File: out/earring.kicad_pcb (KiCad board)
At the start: 6 copper layers, 30.5 x 35.8 mm, 120 parts, among them J1 USB-C, SW1 BOOTSEL, SW2 PWR, U1 RP2354A, U2 LGS4056H, U3 NCP730-3.3, U4 TPS22913, U5 USBLC6-2P6, U6 LSM6DS3TR-C, Y1 12MHz

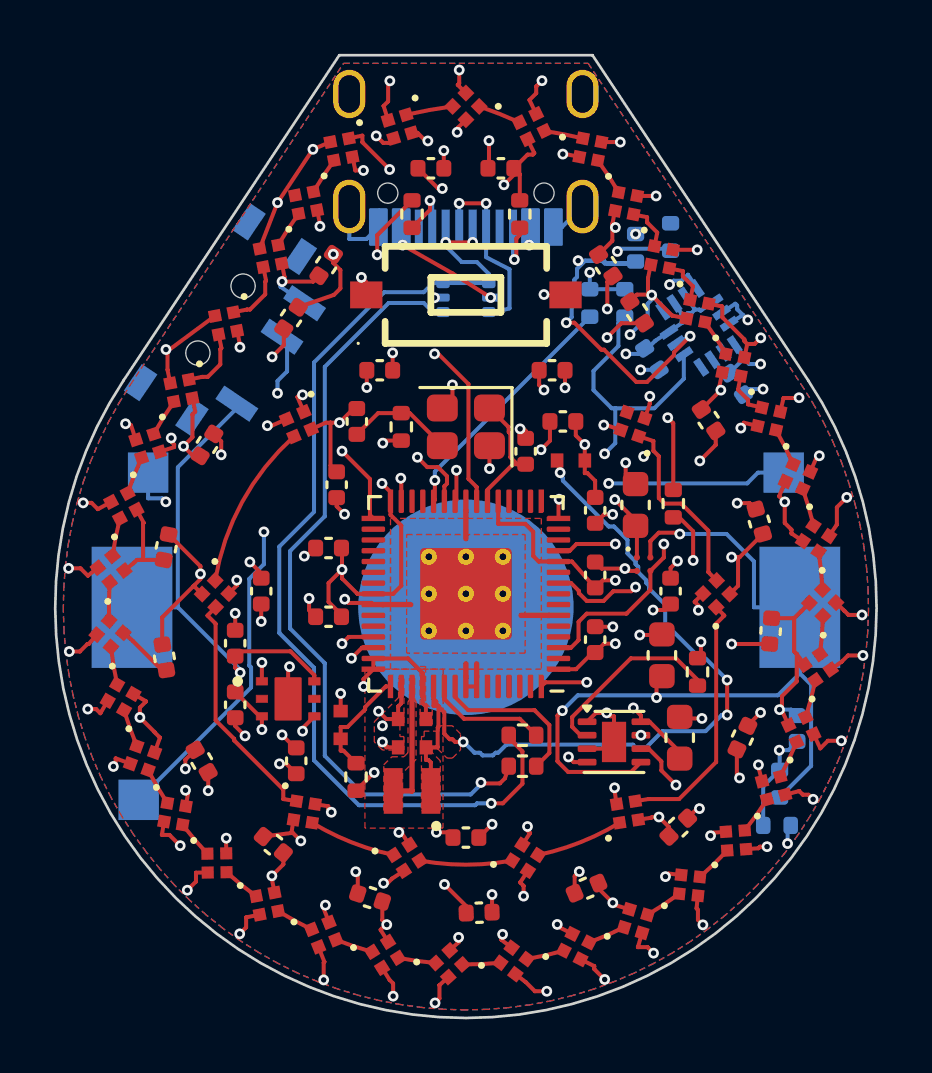
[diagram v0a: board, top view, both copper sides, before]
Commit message: PARTIAL 4-layer board: 0 DRC errors, 8 nets left to hand-route
*** This board is NOT fully routed. It is the best of 6 auto-routing
*** attempts and is handed over for manual completion. See
*** docs/PUNCHLIST-4layer.md.

- design.yaml: layers 4 (was 6) for JLC lead time. The whole pipeline
  switches on board.layers now — route.py (In3/In4 zones, In2 annulus
  hole pulled to r9.35 + 3V3 disc to r9.15 so the interior LED ring
  still gets a plane drop), finish.py (per-stackup plane bands),
  render.py + export.py (layer lists). Set it back to 6 to fall back.
- finish.py: keep_if_best() snapshots the best attempt to
  out/earring-best{.kicad_pcb,.json}. build.py re-rolls the freerouting
  seed on failure and overwrote the board every attempt, so the LAST
  result survived rather than the best one — which is precisely the
  thing worth keeping when a stackup can't be closed automatically.
  build.py clears stale snapshots at the start of a run so a previous
  netlist's score can't veto this one's.
- The In3 east-pour polygon is now defined once in finish.py and
  imported by route.py (was duplicated with a 'keep in sync' comment).

Attempts: 9 / 8 / 11 / 8 / 11 / 11 unconnected, all 0 errors. Stranded:
the three QSPI signals that lost the In3 layer (SD0/SD1/SCLK), the two
back-to-front hops that also used it (LED_EN, IMU_INT1), and three short
local ones (USB_DM, USB_DP, XIN).

Co-Authored-By: Claude Fable 5 <noreply@anthropic.com>
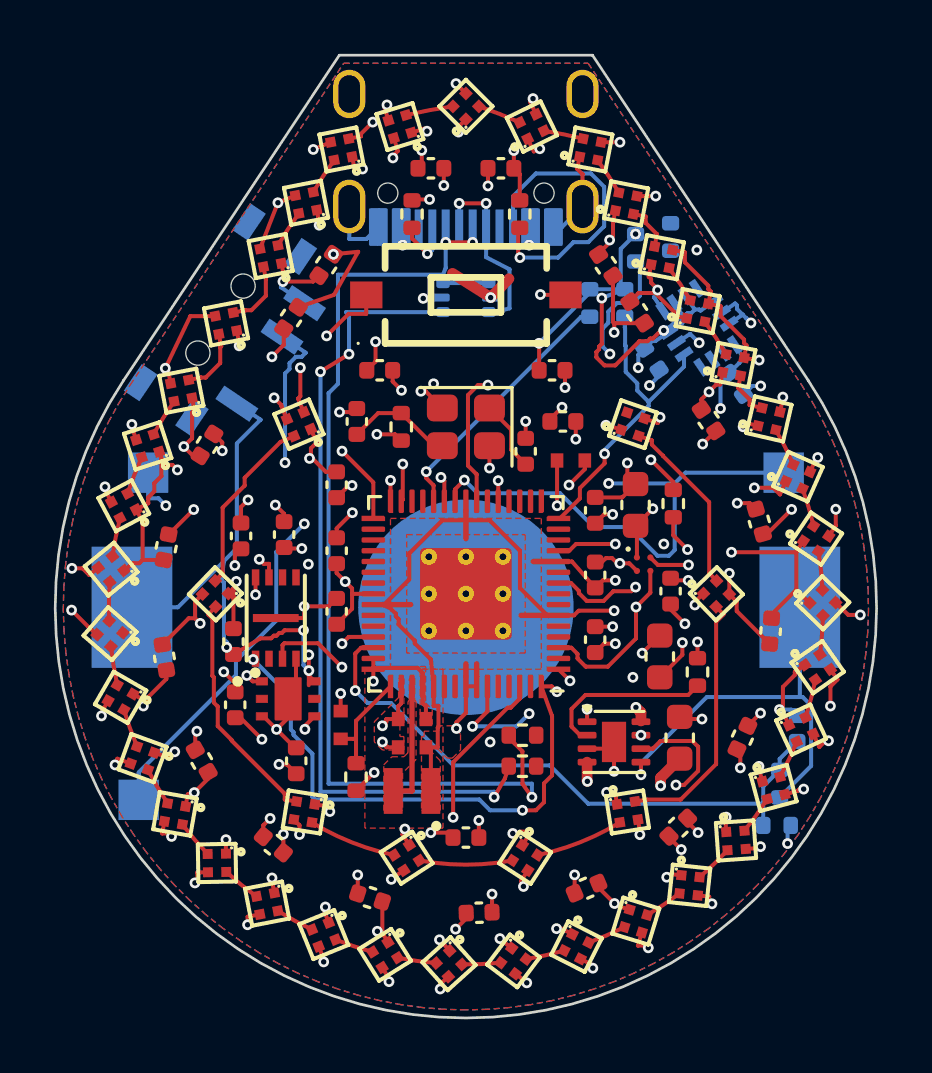
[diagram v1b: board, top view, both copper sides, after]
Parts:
- added C25: 100n, C_0402_1005Metric, F.Cu at (93.2, 97.3)
- added U7: W25Q16JVUXIQ, USON-8_L3.0-W2.0-P0.50-BL-EP, F.Cu at (92.9, 100.4)
- LED1, LED10, LED11, LED12, LED13, LED14, LED15, LED16, LED17, LED18, LED19, LED2, LED20, LED21, LED22, LED23, LED24, LED25, LED26, LED27, LED28, LED29, LED3, LED30, LED31, LED32, LED33, LED34, LED35, LED36, LED37, LED38, LED39, LED4, LED40, LED41, LED42, LED43, LED44, LED45, LED5, LED6, LED7, LED8, LED9: value TBA-C1010MB -> SK6805-EC10; footprint LED_TBA-C1010MB -> LED_SK6805-EC10
- U1: value RP2354A -> RP2350A
- moved C68 2.18 mm to (91.7, 97.3)
- moved C5 0.36 mm to (95.2, 100.2), turned to 90 degrees
- moved C3 0.32 mm to (95.2, 97.9), turned to 90 degrees
- moved C17 0.09 mm to (107.2, 101.8)
- moved C18 0.09 mm to (91.4, 101.3)
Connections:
- LED1 pad 1: LED_D0 -> GND
- LED1 pad 2: VLED -> LED_D0
- LED1 pad 3: GND -> VLED
- LED10 pad 1: LED_D9 -> GND
- LED10 pad 2: VLED -> LED_D9
- LED10 pad 3: GND -> VLED
- LED11 pad 1: LED_D10 -> GND
- LED11 pad 2: VLED -> LED_D10
- LED11 pad 3: GND -> VLED
- LED12 pad 1: LED_D11 -> GND
- LED12 pad 2: VLED -> LED_D11
- LED12 pad 3: GND -> VLED
- LED13 pad 1: LED_D12 -> GND
- LED13 pad 2: VLED -> LED_D12
- LED13 pad 3: GND -> VLED
- LED14 pad 1: LED_D13 -> GND
- LED14 pad 2: VLED -> LED_D13
- LED14 pad 3: GND -> VLED
- LED15 pad 1: LED_D14 -> GND
- LED15 pad 2: VLED -> LED_D14
- LED15 pad 3: GND -> VLED
- LED16 pad 1: LED_D15 -> GND
- LED16 pad 2: VLED -> LED_D15
- LED16 pad 3: GND -> VLED
- LED17 pad 1: LED_D16 -> GND
- LED17 pad 2: VLED -> LED_D16
- LED17 pad 3: GND -> VLED
- LED18 pad 1: LED_D17 -> GND
- LED18 pad 2: VLED -> LED_D17
- LED18 pad 3: GND -> VLED
- LED19 pad 1: LED_D18 -> GND
- LED19 pad 2: VLED -> LED_D18
- LED19 pad 3: GND -> VLED
- LED2 pad 1: LED_D1 -> GND
- LED2 pad 2: VLED -> LED_D1
- LED2 pad 3: GND -> VLED
- LED20 pad 1: LED_D19 -> GND
- LED20 pad 2: VLED -> LED_D19
- LED20 pad 3: GND -> VLED
- LED21 pad 1: LED_D20 -> GND
- LED21 pad 2: VLED -> LED_D20
- LED21 pad 3: GND -> VLED
- LED22 pad 1: LED_D21 -> GND
- LED22 pad 2: VLED -> LED_D21
- LED22 pad 3: GND -> VLED
- LED23 pad 1: LED_D22 -> GND
- LED23 pad 2: VLED -> LED_D22
- LED23 pad 3: GND -> VLED
- LED24 pad 1: LED_D23 -> GND
- LED24 pad 2: VLED -> LED_D23
- LED24 pad 3: GND -> VLED
- LED25 pad 1: LED_D24 -> GND
- LED25 pad 2: VLED -> LED_D24
- LED25 pad 3: GND -> VLED
- LED26 pad 1: LED_D25 -> GND
- LED26 pad 2: VLED -> LED_D25
- LED26 pad 3: GND -> VLED
- LED27 pad 1: LED_D26 -> GND
- LED27 pad 2: VLED -> LED_D26
- LED27 pad 3: GND -> VLED
- LED28 pad 1: LED_D27 -> GND
- LED28 pad 2: VLED -> LED_D27
- LED28 pad 3: GND -> VLED
- LED29 pad 1: LED_D28 -> GND
- LED29 pad 2: VLED -> LED_D28
- LED29 pad 3: GND -> VLED
- LED3 pad 1: LED_D2 -> GND
- LED3 pad 2: VLED -> LED_D2
- LED3 pad 3: GND -> VLED
- LED30 pad 1: LED_D29 -> GND
- LED30 pad 2: VLED -> LED_D29
- LED30 pad 3: GND -> VLED
- LED31 pad 1: LED_D30 -> GND
- LED31 pad 2: VLED -> LED_D30
- LED31 pad 3: GND -> VLED
- LED32 pad 1: LED_D31 -> GND
- LED32 pad 2: VLED -> LED_D31
- LED32 pad 3: GND -> VLED
- LED33 pad 1: LED_D32 -> GND
- LED33 pad 2: VLED -> LED_D32
- LED33 pad 3: GND -> VLED
- LED34 pad 1: LED_D33 -> GND
- LED34 pad 2: VLED -> LED_D33
- LED34 pad 3: GND -> VLED
- LED35 pad 1: LED_D34 -> GND
- LED35 pad 2: VLED -> LED_D34
- LED35 pad 3: GND -> VLED
- LED36 pad 1: LED_D35 -> GND
- LED36 pad 2: VLED -> LED_D35
- LED36 pad 3: GND -> VLED
- LED37 pad 1: LED_D36 -> GND
- LED37 pad 2: VLED -> LED_D36
- LED37 pad 3: GND -> VLED
- LED38 pad 1: LED_D37 -> GND
- LED38 pad 2: VLED -> LED_D37
- LED38 pad 3: GND -> VLED
- LED39 pad 1: LED_D38 -> GND
- LED39 pad 2: VLED -> LED_D38
- LED39 pad 3: GND -> VLED
- LED4 pad 1: LED_D3 -> GND
- LED4 pad 2: VLED -> LED_D3
- LED4 pad 3: GND -> VLED
- LED40 pad 1: LED_D39 -> GND
- LED40 pad 2: VLED -> LED_D39
- LED40 pad 3: GND -> VLED
- LED41 pad 1: LED_D40 -> GND
- LED41 pad 2: VLED -> LED_D40
- LED41 pad 3: GND -> VLED
- LED42 pad 1: LED_D41 -> GND
- LED42 pad 2: VLED -> LED_D41
- LED42 pad 3: GND -> VLED
- LED43 pad 1: LED_D42 -> GND
- LED43 pad 2: VLED -> LED_D42
- LED43 pad 3: GND -> VLED
- LED44 pad 1: LED_D43 -> GND
- LED44 pad 2: VLED -> LED_D43
- LED44 pad 3: GND -> VLED
- LED45 pad 1: LED_D44 -> GND
- LED45 pad 2: VLED -> LED_D44
- LED45 pad 3: GND -> VLED
- LED5 pad 1: LED_D4 -> GND
- LED5 pad 2: VLED -> LED_D4
- LED5 pad 3: GND -> VLED
- LED6 pad 1: LED_D5 -> GND
- LED6 pad 2: VLED -> LED_D5
- LED6 pad 3: GND -> VLED
- LED7 pad 1: LED_D6 -> GND
- LED7 pad 2: VLED -> LED_D6
- LED7 pad 3: GND -> VLED
- LED8 pad 1: LED_D7 -> GND
- LED8 pad 2: VLED -> LED_D7
- LED8 pad 3: GND -> VLED
- LED9 pad 1: LED_D8 -> GND
- LED9 pad 2: VLED -> LED_D8
- LED9 pad 3: GND -> VLED
- U1 pad 55: (no net) -> QSPI_SD3
- U1 pad 56: (no net) -> QSPI_SCLK
- U1 pad 57: (no net) -> QSPI_SD0
- U1 pad 58: (no net) -> QSPI_SD2
- U1 pad 59: (no net) -> QSPI_SD1
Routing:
- net BOOTSEL: track 10.7 -> 30.3 mm, vias 2 -> 4
- net QSPI_SD3: track 0.00 -> 17.4 mm, vias 0 -> 3
- net 3V3: track 44.0 -> 61.1 mm, vias 18 -> 27
- net QSPI_SD2: track 0.00 -> 17.1 mm, vias 0 -> 2
- net IMU_INT1: track 14.4 -> 2.22 mm, vias 2 -> 1
- net LED_EN: track 20.4 -> 9.20 mm
- net IMU_SDA: track 30.8 -> 21.7 mm, vias 4 -> 3
- net CC2: track 2.49 -> 11.3 mm
- net USB_DP: track 6.06 -> 0.00 mm
- net GND: track 107.6 -> 113.2 mm, vias 78 -> 80
- net VLED: track 85.4 -> 80.3 mm, vias 60 -> 62
- net SWCLK: track 14.2 -> 19.1 mm
- net CHRG: track 20.7 -> 25.3 mm
- net USB_DM: track 4.44 -> 0.00 mm
- net XIN: track 5.06 -> 2.64 mm
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- removed copper zone on In3.Cu, net 3V3
- removed copper zone on In3.Cu, net VDD_CORE
- removed copper zone on In4.Cu, net VLED
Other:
- copper layers 6 -> 4

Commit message: Link schematic to PCB: footprint properties, UUID paths, fp-lib-table
Fixes 'Cannot update <ref> (no footprint assigned)' on Update PCB from
Schematic. Four things were missing:

- Symbols had no Footprint property. Each now carries
  'earring:<footprint>' taken from bom/parts.yaml via circuit.py.
- No fp-lib-table, so that nickname resolved to nothing. gen_board.py
  writes out/fp-lib-table pointing at library/parts.pretty (tracked).
- Board footprints had bare FPIDs and empty paths, so KiCad could not
  tell that board R10 IS schematic R10. gen_board.py now stamps the
  library nickname and the schematic symbol's UUID path; both sides
  derive UUIDs deterministically, so neither has to run first.
- The project file listed no root sheet ('sheets': []).

The bigger fix: the schematic is now COMPLETE. The 45-LED chain and the
bypass-cap banks were collapsed to representatives plus a note, which
reads well but is wrong for a sheet that drives the board — KiCad
offers to DELETE any footprint with no matching symbol, so the 41
undrawn LEDs and 23 ring caps were at risk. They are drawn in full as
grids (page A2 -> A1), with an assert that every component is placed.
Unused pins get no-connect flags instead of dangling.

The existing PARTIAL board was patched in place, NOT regenerated:
1363 tracks before and after, DRC unchanged at 0 errors / 8 unconnected.

Verified: kicad-cli sch erc = 0 violations; netlist export = 122/122
components with footprints; cross-check of every board footprint
against its symbol = 0 path/footprint/orphan mismatches.

Co-Authored-By: Claude Fable 5 <noreply@anthropic.com>
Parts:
- BT1: footprint BAT_CR2032_W -> earring:BAT_CR2032_W
- C1, C14, C15, C18, C19, C2, C21, C23, C24, C25, C3, C30, C32, C34, C36, C38, C4, C40, C42, C44, C46, C48, C5, C50, C52, C54, C56, C58, C6, C60, C62, C64, C66, C68, C7, C70, C72, C74, C8, C9: footprint C_0402_1005Metric -> earring:C_0402_1005Metric
- C11, C12, C13, C22: footprint C_0402_1005Metric_small_pads -> earring:C_0402_1005Metric_small_pads
- C16, C17, C20: footprint C_0603_1608Metric -> earring:C_0603_1608Metric
- J1: footprint USB-C_SMD-TYPE-C-31-M-12_1 -> earring:USB-C_SMD-TYPE-C-31-M-12_1
- L1: footprint L_pol_2016 -> earring:L_pol_2016
- LED1, LED10, LED11, LED12, LED13, LED14, LED15, LED16, LED17, LED18, LED19, LED2, LED20, LED21, LED22, LED23, LED24, LED25, LED26, LED27, LED28, LED29, LED3, LED30, LED31, LED32, LED33, LED34, LED35, LED36, LED37, LED38, LED39, LED4, LED40, LED41, LED42, LED43, LED44, LED45, LED5, LED6, LED7, LED8, LED9: footprint LED_SK6805-EC10 -> earring:LED_SK6805-EC10
- R1, R10, R11, R12, R13, R14, R15, R2, R3, R4, R5, R6, R7, R8: footprint R_0402_1005Metric -> earring:R_0402_1005Metric
- SW1: footprint SW-SMD_L6.0-W3.3-LS8.0_TS-1101-C-W -> earring:SW-SMD_L6.0-W3.3-LS8.0_TS-1101-C-W
- SW2: footprint SW-TH_MSK12C02 -> earring:SW-TH_MSK12C02
- TP1, TP2, TP3: footprint TestPoint_Pad_1.5x1.5mm -> earring:TestPoint_Pad_1.5x1.5mm
- U1: footprint RP2350-QFN-60-1EP_7x7_P0.4mm_EP3.4x3.4mm_ThermalVias -> earring:RP2350-QFN-60-1EP_7x7_P0.4mm_EP3.4x3.4mm_ThermalVias
- U2: footprint DFN-8-1EP_2x2mm_P0.5mm_EP0.9x1.5mm -> earring:DFN-8-1EP_2x2mm_P0.5mm_EP0.9x1.5mm
- U3: footprint WDFN-6-2x2 -> earring:WDFN-6-2x2
- U4: footprint YZV0004ADAD -> earring:YZV0004ADAD
- U5: footprint SOT-666 -> earring:SOT-666
- U6: footprint LGA-14_L3.0-W2.5-P0.50-TL -> earring:LGA-14_L3.0-W2.5-P0.50-TL
- U7: footprint USON-8_L3.0-W2.0-P0.50-BL-EP -> earring:USON-8_L3.0-W2.0-P0.50-BL-EP
- Y1: footprint Crystal_SMD_2520-4Pin_2.5x2.0mm -> earring:Crystal_SMD_2520-4Pin_2.5x2.0mm

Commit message: Save latest PCB/schematic edits from KiCad; add BOOTSEL switch 3D model
Hand-routing progress on out/earring.kicad_pcb plus KiCad's resave of the
schematic and project file. Adds parts/ with the WRL model for the
KEY-SMD_4P-L4.2-W3.2-P2.20-LS4.6 tactile switch.

Co-Authored-By: Claude Fable 5 <noreply@anthropic.com>
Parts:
- R6, R7: moved to B.Cu
- moved R6 17.4 mm to (97.4, 89.1), turned to 180 degrees
- moved R7 17.4 mm to (97.4, 88.0), turned to 180 degrees
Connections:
- net USB_DM renamed USB_DN
- J1 pad A8: (no net) -> unconnected-(J1-PadA8)
- J1 pad B8: (no net) -> unconnected-(J1-PadB8)
- LED45 pad 4: (no net) -> unconnected-(LED45-DOUT-Pad4)
- U1 pad 10: (no net) -> unconnected-(U1-GPIO7-Pad10)
- U1 pad 13: (no net) -> unconnected-(U1-GPIO9-Pad13)
- U1 pad 14: (no net) -> unconnected-(U1-GPIO10-Pad14)
- U1 pad 16: (no net) -> unconnected-(U1-GPIO12-Pad16)
- U1 pad 17: (no net) -> unconnected-(U1-GPIO13-Pad17)
- U1 pad 18: (no net) -> unconnected-(U1-GPIO14-Pad18)
- U1 pad 19: (no net) -> unconnected-(U1-GPIO15-Pad19)
- U1 pad 2: (no net) -> unconnected-(U1-GPIO0-Pad2)
- U1 pad 27: (no net) -> unconnected-(U1-GPIO16-Pad27)
- U1 pad 28: (no net) -> unconnected-(U1-GPIO17-Pad28)
- U1 pad 32: (no net) -> unconnected-(U1-GPIO20-Pad32)
- U1 pad 33: (no net) -> unconnected-(U1-GPIO21-Pad33)
- U1 pad 34: (no net) -> unconnected-(U1-GPIO22-Pad34)
- U1 pad 35: (no net) -> unconnected-(U1-GPIO23-Pad35)
- U1 pad 36: (no net) -> unconnected-(U1-GPIO24-Pad36)
- U1 pad 37: (no net) -> unconnected-(U1-GPIO25-Pad37)
- U1 pad 4: (no net) -> unconnected-(U1-GPIO2-Pad4)
- U1 pad 40: (no net) -> unconnected-(U1-GPIO26-Pad40)
- U1 pad 41: (no net) -> unconnected-(U1-GPIO27-Pad41)
- U1 pad 5: (no net) -> unconnected-(U1-GPIO3-Pad5)
- U1 pad 7: (no net) -> unconnected-(U1-GPIO4-Pad7)
- U1 pad 8: (no net) -> unconnected-(U1-GPIO5-Pad8)
- U3 pad 2: (no net) -> unconnected-(U3-GND-Pad2)
- U3 pad 5: (no net) -> unconnected-(U3-OUT-Pad5)
- U6 pad 10: (no net) -> unconnected-(U6-GND-Pad10)
- U6 pad 11: (no net) -> unconnected-(U6-INT1-Pad11)
- U6 pad 9: (no net) -> unconnected-(U6-GND-Pad9)
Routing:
- net USB_C_DN: track 39.0 -> 7.07 mm, vias 3 -> 2
- net USB_C_DP: track 39.2 -> 10.2 mm, vias 5 -> 2
- net USB_DN: track 0.00 -> 24.5 mm, vias 0 -> 1
- net USB_DP: track 0.00 -> 23.4 mm, vias 0 -> 1
- net QSPI_SD1: track 0.00 -> 16.0 mm, vias 0 -> 2
- net LED_EN: track 9.20 -> 23.2 mm, vias 2 -> 3
- net QSPI_SCLK: track 0.00 -> 13.4 mm, vias 0 -> 2
- net QSPI_SD0: track 0.00 -> 13.0 mm, vias 0 -> 2
- net IMU_INT1: track 2.22 -> 14.1 mm, vias 1 -> 2
- net SWCLK: track 19.1 -> 13.5 mm, vias 2 -> 1
- net QSPI_SD3: track 17.4 -> 13.4 mm, vias 3 -> 2
- net VBUS: track 41.9 -> 39.3 mm
- net XIN: track 2.64 -> 4.89 mm
- net VBSENSE: track 22.7 -> 24.5 mm
- net 3V3: track 61.1 -> 62.5 mm
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
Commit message: BOOTSEL: swap TS-1101-C-W for SKRPAME010 (C19724063), 4-pin tact
Smaller part: pads move from (+-3.70, 0) to (+-2.10, +-1.07), body
4.2x3.2mm vs 6.0x3.3mm. Footprint pulled via easyeda2kicad into
library/parts.pretty; 3D model is the vendor WRL in parts/ with the
mm -> 0.1in scale (x0.3937) BAKED INTO ITS VERTICES, so the footprint
keeps (scale 1 1 1) -- KiCad's scale field has export issues.

circuit.py: SW1 is now 4 pads, 1-2 = BOOTSEL_SW and 3-4 = GND (per the
LCSC symbol; confirm against the ALPS drawing before ordering).
Schematic regenerated. PCB footprint swapped in place via pcbnew,
keeping position, rotation, reference and the schematic UUID path;
Sequoia rerouted the CC1/CC2 collisions the new pad positions caused.

DRC: 3 errors left, all on the LED ring (VLED via shorting the LED_D41
arc), none from SW1. 0 unconnected.

Co-Authored-By: Claude Fable 5 <noreply@anthropic.com>
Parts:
- SW1: footprint earring:SW-SMD_L6.0-W3.3-LS8.0_TS-1101-C-W -> earring:KEY-SMD_4P-L4.2-W3.2-P2.20-LS4.6
- moved TP3 0.62 mm to (88.5, 107.0)
- moved SW1 0.40 mm to (100.0, 88.8)
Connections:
- net USB_DN renamed USB_DM
- SW1 pad 2: GND -> BOOTSEL_SW
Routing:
- net VBUS: track 39.3 -> 60.5 mm
- net CC2: track 11.3 -> 2.40 mm
- net BOOTSEL_SW: track 18.0 -> 23.8 mm
- net GND: track 113.6 -> 118.9 mm
- net 3V3: track 62.5 -> 58.7 mm
- net VDD_CORE: track 31.8 -> 30.2 mm
- net LED_D37: track 12.6 -> 14.2 mm
- net BOOTSEL: track 30.3 -> 29.4 mm
- net VLED: track 81.2 -> 80.4 mm
- net PWR_EN: track 16.6 -> 15.8 mm
- net CHRG: track 25.9 -> 25.4 mm
- net LED_D0: track 16.3 -> 16.4 mm, vias 2 -> 3
